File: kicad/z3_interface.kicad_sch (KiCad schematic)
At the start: 0 parts

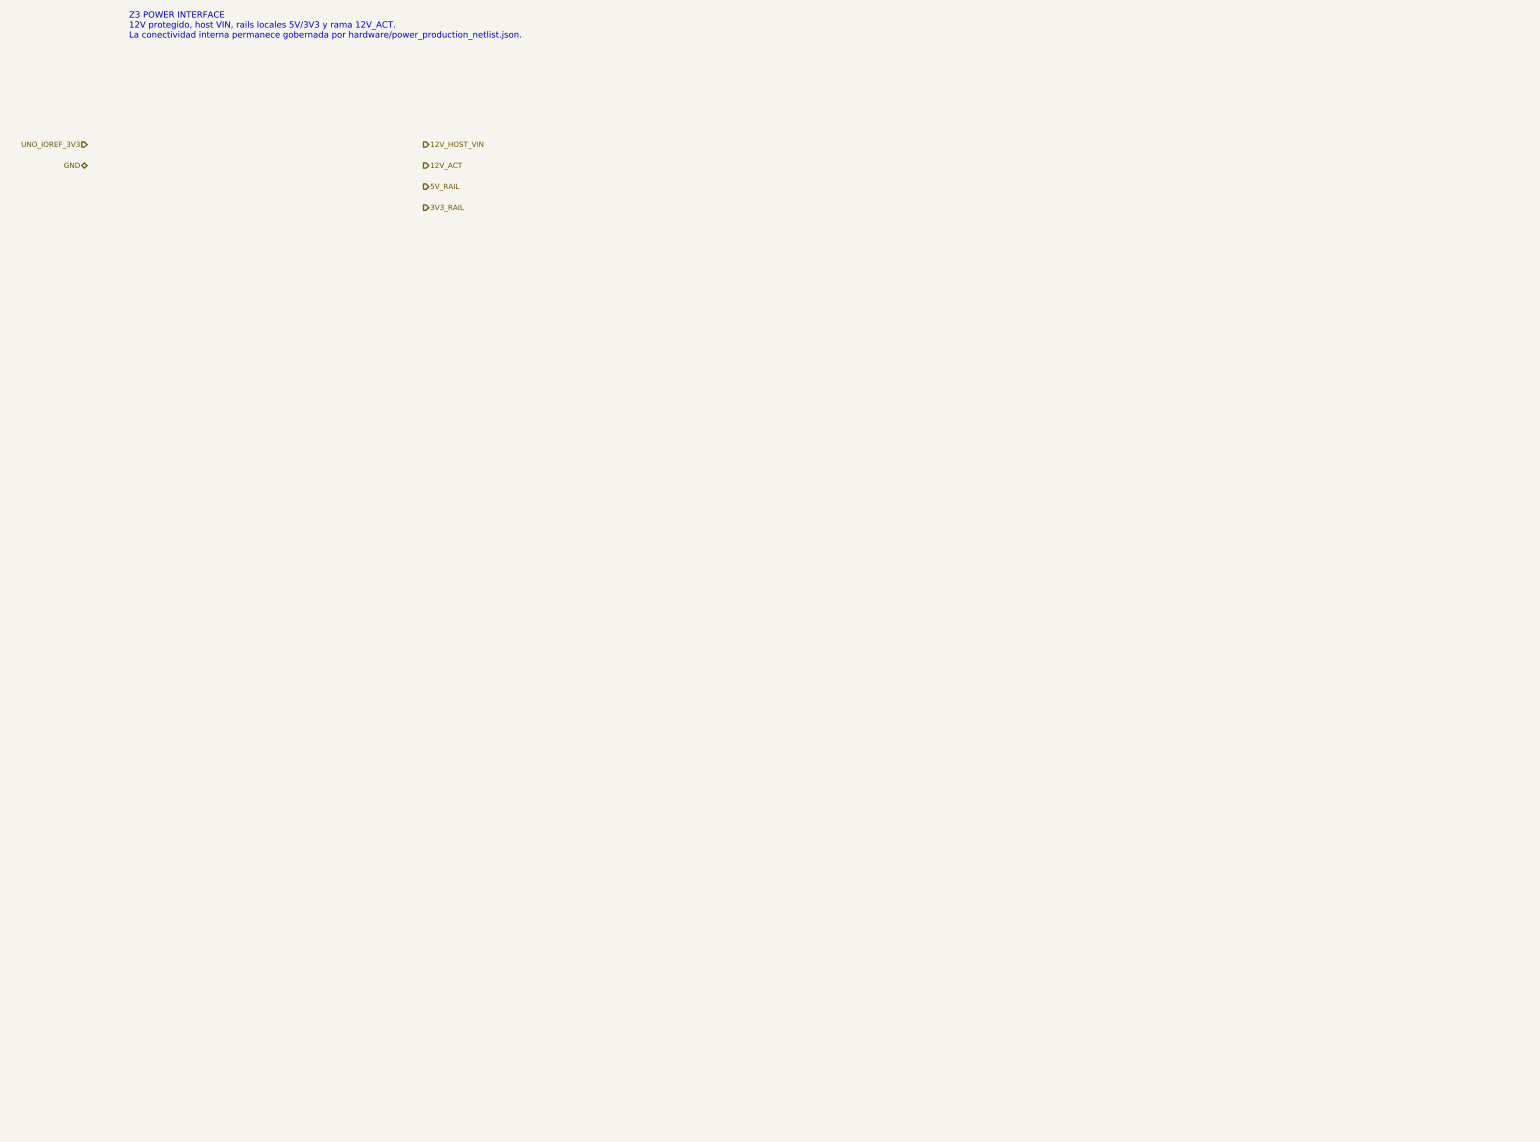
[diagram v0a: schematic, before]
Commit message: eda: materializar hierarchy de producción y cerrar ERC en cero (#15)
Materializa Z0–Z4 de forma determinista desde JSON/BOM, registra NFB_GEN, cierra seis links físicos verificados, elimina la deuda ERC de PR #14 y congela ERC=0/0 antes de placement. Mantiene placement, routing y geometría PCB fuera de alcance.
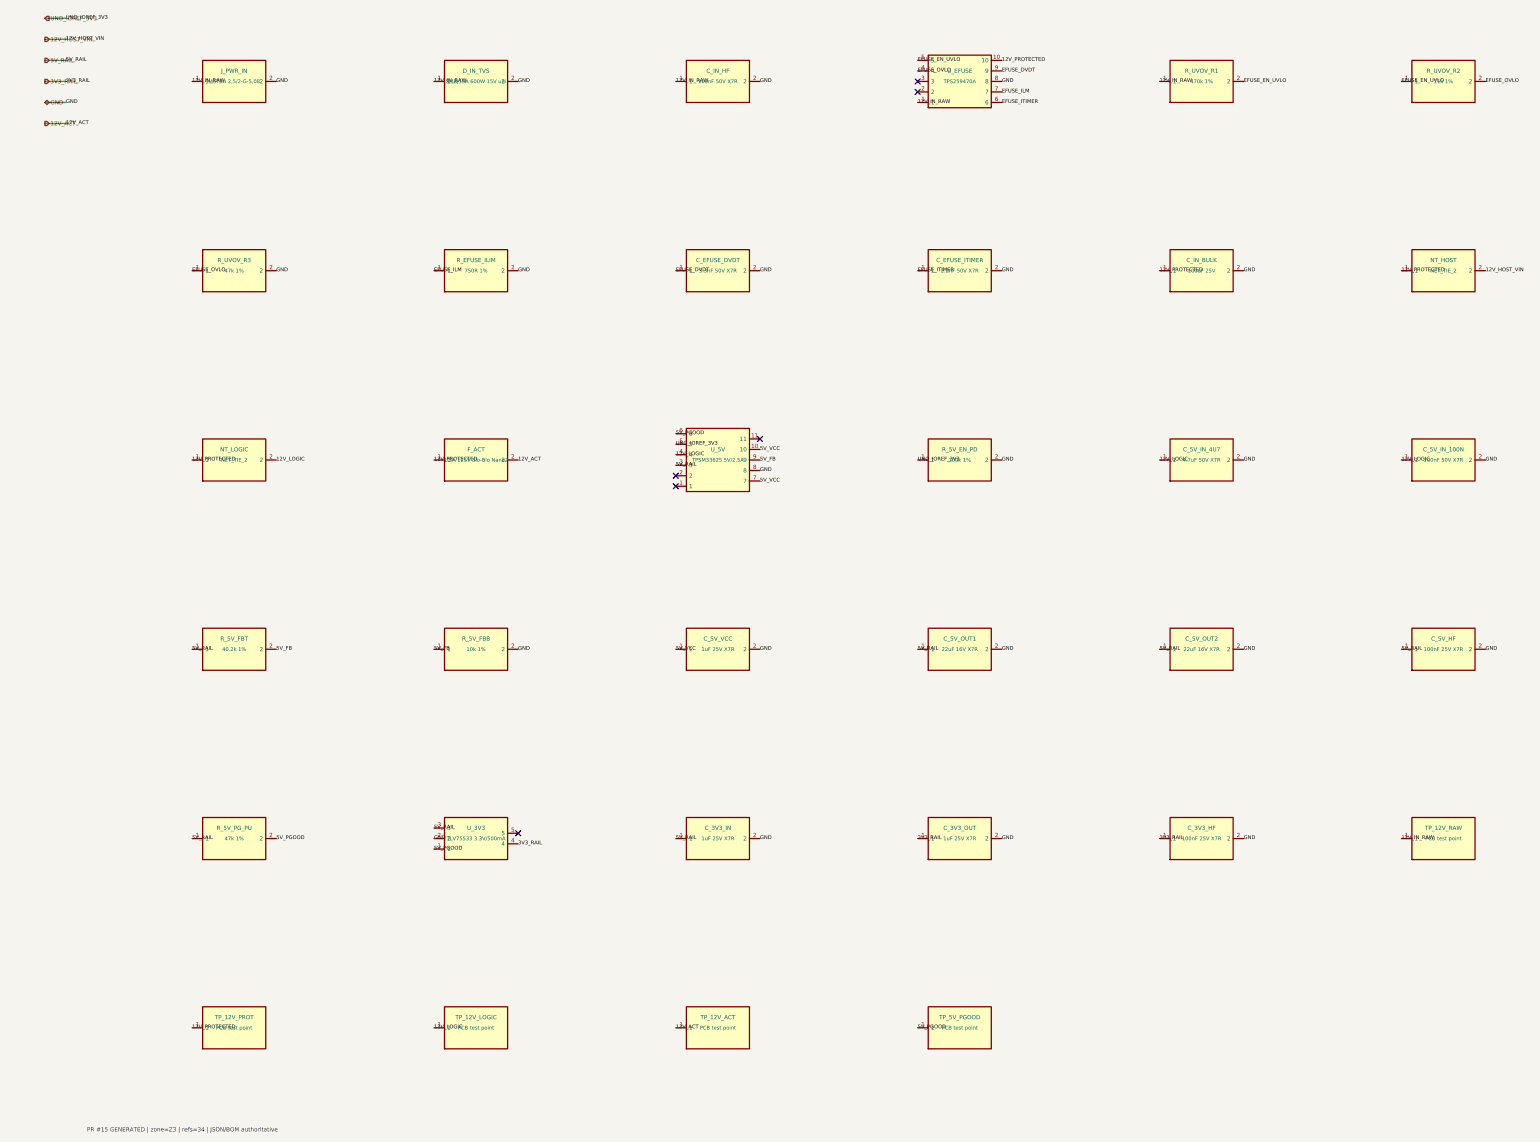
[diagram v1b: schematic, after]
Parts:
- added C_3V3_HF: 100nF 25V X7R, Capacitor_SMD:C_0402_1005Metric, symbol NFB_GEN:SYM_C_3V3_HF
- added C_3V3_IN: 1uF 25V X7R, Capacitor_SMD:C_0603_1608Metric, symbol NFB_GEN:SYM_C_3V3_IN
- added C_3V3_OUT: 1uF 25V X7R, Capacitor_SMD:C_0603_1608Metric, symbol NFB_GEN:SYM_C_3V3_OUT
- added C_5V_HF: 100nF 25V X7R, Capacitor_SMD:C_0402_1005Metric, symbol NFB_GEN:SYM_C_5V_HF
- added C_5V_IN_100N: 100nF 50V X7R, Capacitor_SMD:C_0603_1608Metric, symbol NFB_GEN:SYM_C_5V_IN_100N
- added C_5V_IN_4U7: 4.7uF 50V X7R, Capacitor_SMD:C_1210_3225Metric, symbol NFB_GEN:SYM_C_5V_IN_4U7
- added C_5V_OUT1: 22uF 16V X7R, Capacitor_SMD:C_1210_3225Metric, symbol NFB_GEN:SYM_C_5V_OUT1
- added C_5V_OUT2: 22uF 16V X7R, Capacitor_SMD:C_1210_3225Metric, symbol NFB_GEN:SYM_C_5V_OUT2
- added C_5V_VCC: 1uF 25V X7R, Capacitor_SMD:C_0603_1608Metric, symbol NFB_GEN:SYM_C_5V_VCC
- added C_EFUSE_DVDT: 3.3nF 50V X7R, Capacitor_SMD:C_0402_1005Metric, symbol NFB_GEN:SYM_C_EFUSE_DVDT
- added C_EFUSE_ITIMER: 2.2nF 50V X7R, Capacitor_SMD:C_0402_1005Metric, symbol NFB_GEN:SYM_C_EFUSE_ITIMER
- added C_IN_BULK: 100uF 25V, Capacitor_SMD:CP_Elec_8x6.2, symbol NFB_GEN:SYM_C_IN_BULK
- added C_IN_HF: 100nF 50V X7R, Capacitor_SMD:C_0603_1608Metric, symbol NFB_GEN:SYM_C_IN_HF
- added D_IN_TVS: SMBJ15A 600W 15V uni, Diode_SMD:D_SMB, symbol NFB_GEN:SYM_D_IN_TVS
- added F_ACT: 1.5A 125V Slo-Blo Nano2, NFB:Littelfuse_0454_NANO2, symbol NFB_GEN:SYM_F_ACT
- added J_PWR_IN: MSTBA 2,5/2-G-5,08, Connector_Phoenix_MSTB:PhoenixContact_MSTBA_2,5_2-G-5,08_1x02_P5.08mm_Horizontal, symbol NFB_GEN:SYM_J_PWR_IN
- added NT_HOST: NET_TIE_2, NetTie:NetTie-2_SMD_Pad0.5mm, symbol NFB_GEN:SYM_NT_HOST
- added NT_LOGIC: NET_TIE_2, NetTie:NetTie-2_SMD_Pad0.5mm, symbol NFB_GEN:SYM_NT_LOGIC
- added R_5V_EN_PD: 100k 1%, Resistor_SMD:R_0402_1005Metric, symbol NFB_GEN:SYM_R_5V_EN_PD
- added R_5V_FBB: 10k 1%, Resistor_SMD:R_0402_1005Metric, symbol NFB_GEN:SYM_R_5V_FBB
- added R_5V_FBT: 40.2k 1%, Resistor_SMD:R_0402_1005Metric, symbol NFB_GEN:SYM_R_5V_FBT
- added R_5V_PG_PU: 47k 1%, Resistor_SMD:R_0402_1005Metric, symbol NFB_GEN:SYM_R_5V_PG_PU
- added R_EFUSE_ILIM: 750R 1%, Resistor_SMD:R_0402_1005Metric, symbol NFB_GEN:SYM_R_EFUSE_ILIM
- added R_UVOV_R1: 470k 1%, Resistor_SMD:R_0402_1005Metric, symbol NFB_GEN:SYM_R_UVOV_R1
- added R_UVOV_R2: 11k 1%, Resistor_SMD:R_0402_1005Metric, symbol NFB_GEN:SYM_R_UVOV_R2
- added R_UVOV_R3: 47k 1%, Resistor_SMD:R_0402_1005Metric, symbol NFB_GEN:SYM_R_UVOV_R3
- added TP_12V_ACT: PCB test point, TestPoint:TestPoint_Pad_D1.0mm, symbol NFB_GEN:SYM_TP_12V_ACT
- added TP_12V_LOGIC: PCB test point, TestPoint:TestPoint_Pad_D1.0mm, symbol NFB_GEN:SYM_TP_12V_LOGIC
- added TP_12V_PROT: PCB test point, TestPoint:TestPoint_Pad_D1.0mm, symbol NFB_GEN:SYM_TP_12V_PROT
- added TP_12V_RAW: PCB test point, TestPoint:TestPoint_Pad_D1.0mm, symbol NFB_GEN:SYM_TP_12V_RAW
- added TP_5V_PGOOD: PCB test point, TestPoint:TestPoint_Pad_D1.0mm, symbol NFB_GEN:SYM_TP_5V_PGOOD
- added U_3V3: TLV75533 3.3V/500mA, Package_TO_SOT_SMD:SOT-23-5, symbol NFB_GEN:SYM_U_3V3
- added U_5V: TPSM33625 5V/2.5A, NFB:TI_RDN0011A_TPSM33625, symbol NFB_GEN:SYM_U_5V
- added U_EFUSE: TPS259470A, NFB:TI_RPW0010A_TPS259470A, symbol NFB_GEN:SYM_U_EFUSE
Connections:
- net 12V_ACT: now also F_ACT.2, TP_12V_ACT.1
- net 12V_HOST_VIN: now also NT_HOST.2
- net 3V3_RAIL: now also C_3V3_HF.1, C_3V3_OUT.1, U_3V3.4
- net 5V_RAIL: now also C_3V3_IN.1, C_5V_HF.1, C_5V_OUT1.1, C_5V_OUT2.1, R_5V_FBT.1, R_5V_PG_PU.1, U_3V3.3, U_5V.3
- net GND: now also C_3V3_HF.2, C_3V3_IN.2, C_3V3_OUT.2, C_5V_HF.2, C_5V_IN_100N.2, C_5V_IN_4U7.2, C_5V_OUT1.2, C_5V_OUT2.2, C_5V_VCC.2, C_EFUSE_DVDT.2, C_EFUSE_ITIMER.2, C_IN_BULK.2, C_IN_HF.2, D_IN_TVS.2, J_PWR_IN.2, R_5V_EN_PD.2, R_5V_FBB.2, R_EFUSE_ILIM.2, R_UVOV_R3.2, U_3V3.2, U_5V.8, U_EFUSE.8
- net UNO_IOREF_3V3: now also R_5V_EN_PD.1, U_5V.5
- new net 12V_IN_RAW: C_IN_HF.1, D_IN_TVS.1, J_PWR_IN.1, R_UVOV_R1.1, TP_12V_RAW.1, U_EFUSE.1
- new net 12V_LOGIC: C_5V_IN_100N.1, C_5V_IN_4U7.1, NT_LOGIC.2, TP_12V_LOGIC.1, U_5V.4
- new net 12V_PROTECTED: C_IN_BULK.1, F_ACT.1, NT_HOST.1, NT_LOGIC.1, TP_12V_PROT.1, U_EFUSE.10
- new net 5V_FB: R_5V_FBB.1, R_5V_FBT.2, U_5V.9
- new net 5V_PGOOD: R_5V_PG_PU.2, TP_5V_PGOOD.1, U_3V3.1, U_5V.6
- new net 5V_VCC: C_5V_VCC.1, U_5V.10, U_5V.7
- new net EFUSE_DVDT: C_EFUSE_DVDT.1, U_EFUSE.9
- new net EFUSE_EN_UVLO: R_UVOV_R1.2, R_UVOV_R2.1, U_EFUSE.5
- new net EFUSE_ILM: R_EFUSE_ILIM.1, U_EFUSE.7
- new net EFUSE_ITIMER: C_EFUSE_ITIMER.1, U_EFUSE.6
- new net EFUSE_OVLO: R_UVOV_R2.2, R_UVOV_R3.1, U_EFUSE.4
- no-connect marks 0 -> 6
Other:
- note added: "PR #15 GENERATED | zone=Z3 | refs=34 | JSON/BOM authoritative"
- note removed: "Z3 POWER INTERFACE 12V protegido, host VIN, rails locales 5V/3V3 y rama 12V_ACT. La conectividad interna permanece gobernada por hardware/power_production_netlist.json."
- title: NFB Insight PCBA v2 — Z3 Power Interface -> NFB Insight PCBA v2 — Z3 GENERATED PRODUCTION
